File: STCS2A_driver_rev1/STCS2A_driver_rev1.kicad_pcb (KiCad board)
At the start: 2 copper layers, 80 x 60 mm, 38 parts, among them J1 Conn_01x04, J10 Screw_Terminal_01x02, J11 Screw_Terminal_01x02, J12 Screw_Terminal_01x02, J2 Conn_01x02, J3 Conn_01x04, J4 Screw_Terminal_01x02, J5 Screw_Terminal_01x02, J6 Conn_01x04, J7 Screw_Terminal_01x02, J8 Screw_Terminal_01x02, J9 Screw_Terminal_01x02, Q1 IRF9540N, U1 STCS2A, U2 STCS2A, U3 STCS2A, U4 STCS2A

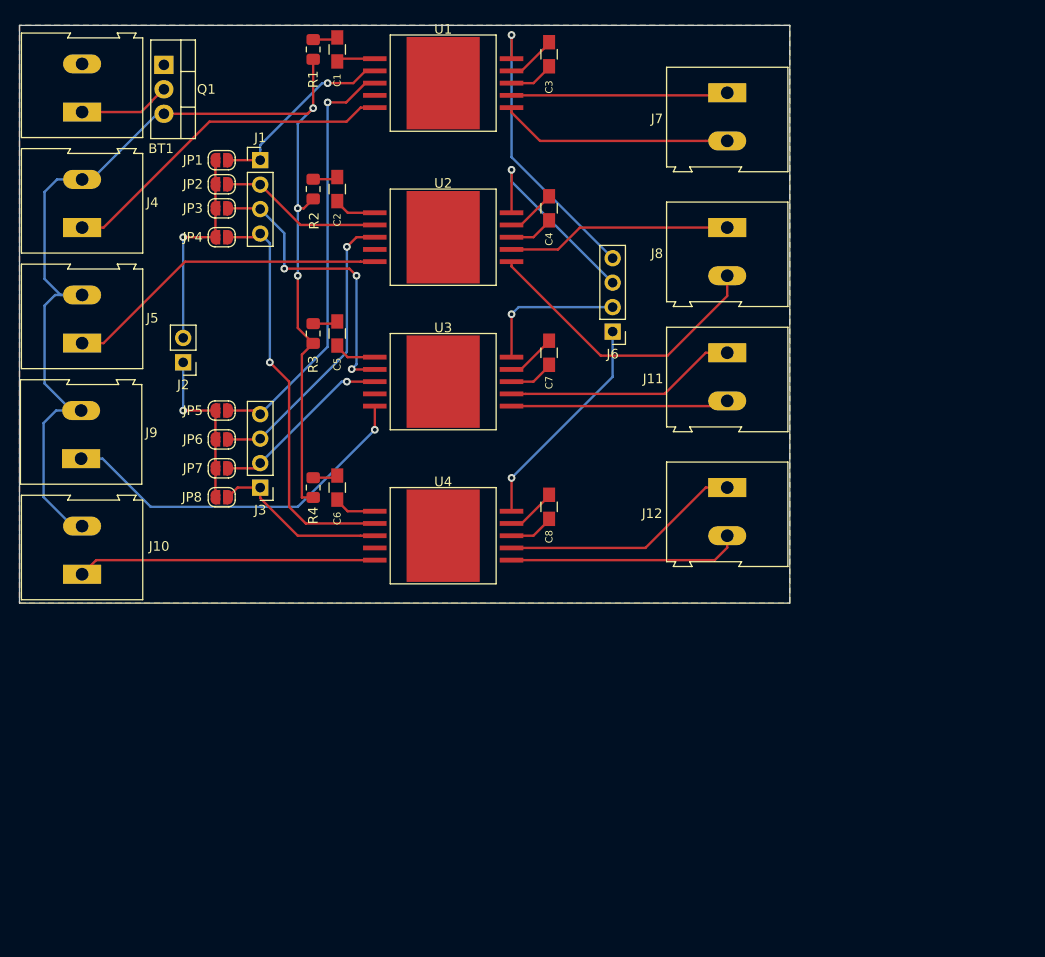
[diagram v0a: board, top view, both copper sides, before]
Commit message: Finished STCS2A driver board
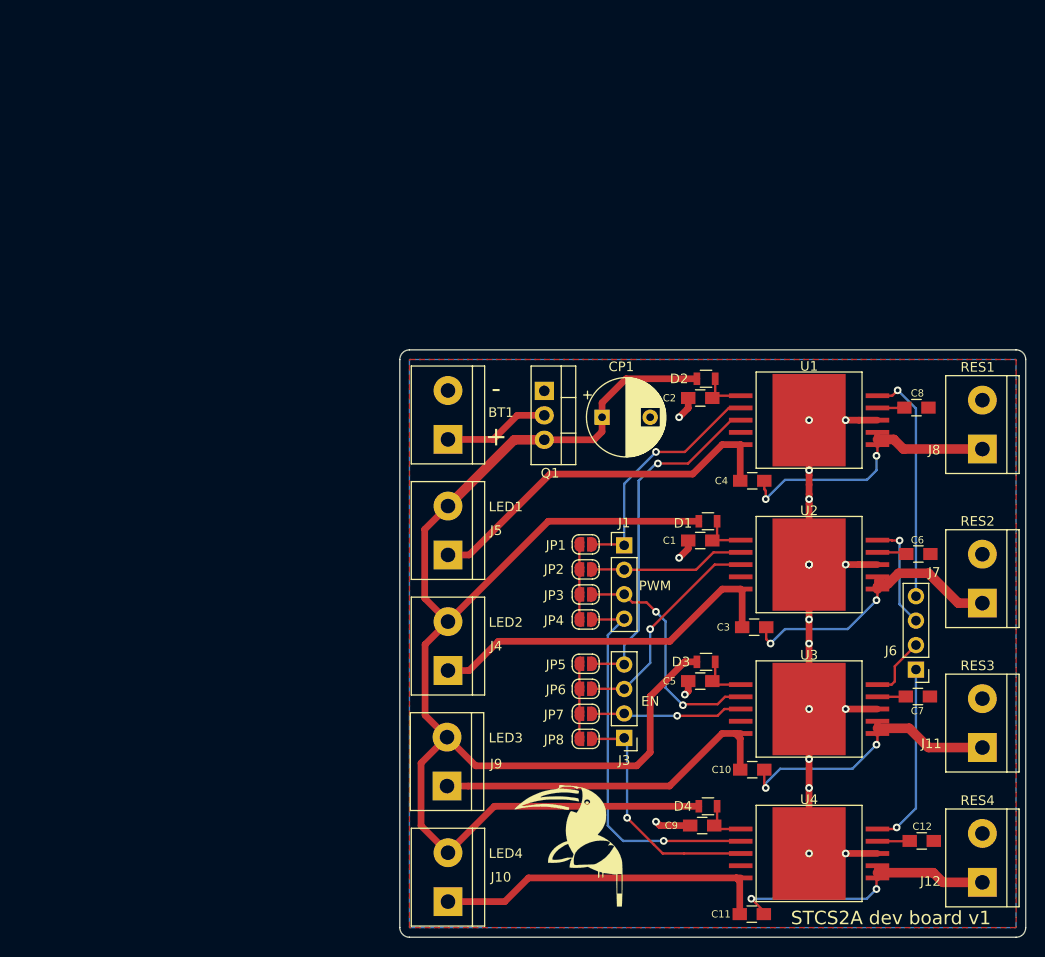
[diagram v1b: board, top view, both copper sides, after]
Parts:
- removed J2: Conn_01x02, Connector_PinHeader_2.54mm:PinHeader_1x02_P2.54mm_Vertical
- removed R1, R2, R3, R4: R, Resistor_SMD:R_0805_2012Metric_Pad1.15x1.40mm_HandSolder
- added C10: 0.47uF, sense_fp:C_0805_HandSoldering, F.Cu at (86.1, 87.3)
- added C11: 0.47uF, sense_fp:C_0805_HandSoldering, F.Cu at (86.0, 102.3)
- added C12: 8pF, sense_fp:C_0805_HandSoldering, F.Cu at (103.7, 94.7)
- added C9: 0.1uF, sense_fp:C_0805_HandSoldering, F.Cu at (80.9, 93.1)
- added CP1: 100uF, sense_fp:CP_Radial_D8.0mm_P5.00mm, F.Cu at (70.5, 50.7)
- added D1: BAT46, sense_fp:R_0805, F.Cu at (81.5, 61.5)
- added D2: BAT46, sense_fp:R_0805, F.Cu at (81.3, 46.7)
- added D3: BAT46, sense_fp:R_0805, F.Cu at (81.3, 76.1)
- added D4: BAT46, sense_fp:R_0805, F.Cu at (81.5, 91.1)
- added G***: Appiko_LOGO_img, sense_fp:Appiko_LOGO_img, F.Cu at (67.0, 95.2)
- BT1: value Battery_Cell -> Battery; footprint TerminalBlock:TerminalBlock_Altech_AK300-2_P5.00mm -> sense_fp:TerminalBlock_bornier-2_P5.08mm
- C1, C2, C5: footprint sense:C_0805_HandSoldering -> sense_fp:C_0805_HandSoldering
- C3, C4: value 10nF -> 0.47uF; footprint sense:C_0805_HandSoldering -> sense_fp:C_0805_HandSoldering
- C6: value 0.1uF -> 8pF; footprint sense:C_0805_HandSoldering -> sense_fp:C_0805_HandSoldering
- C7, C8: value 10nF -> 8pF; footprint sense:C_0805_HandSoldering -> sense_fp:C_0805_HandSoldering
- J1, J3, J6: footprint Connector_PinHeader_2.54mm:PinHeader_1x04_P2.54mm_Vertical -> sense_fp:PinHeader_1x04_P2.54mm_Vertical
- J10, J11, J12, J4, J5, J7, J8, J9: footprint TerminalBlock:TerminalBlock_Altech_AK300-2_P5.00mm -> sense_fp:TerminalBlock_bornier-2_P5.08mm
- JP1, JP2, JP3, JP4, JP5, JP6, JP7, JP8: footprint Jumper:SolderJumper-2_P1.3mm_Open_RoundedPad1.0x1.5mm -> sense_fp:SolderJumper-2_P1.3mm_Open_RoundedPad1.0x1.5mm
- Q1: value IRF9540N -> IRF9540; footprint Package_TO_SOT_THT:TO-220-3_Vertical -> sense_fp:TO-220-3_Vertical
- U1, U2, U3, U4: footprint sense:STCS2A_PowerSO-10 -> sense_fp:STCS2A_PowerSO-10
- moved C1 63.4 mm to (80.7, 63.5), turned to 0 degrees
- moved C3 63.2 mm to (86.3, 72.5), turned to 0 degrees
- moved C6 60.7 mm to (103.3, 64.9), turned to 0 degrees
- moved J4 59.7 mm to (54.5, 77.0)
- moved J7 59.3 mm to (110.0, 70.0), turned to 90 degrees
- moved JP3 55.1 mm to (68.8, 69.1)
- moved J1 55.0 mm to (72.8, 64.0)
- moved JP2 55.0 mm to (68.8, 66.5)
- moved JP1 55.0 mm to (68.8, 63.9)
- moved JP4 54.8 mm to (68.8, 71.7)
- moved C7 52.4 mm to (103.3, 79.7), turned to 0 degrees
- moved C5 52.2 mm to (80.7, 78.1), turned to 0 degrees
- moved Q1 52.0 mm to (64.5, 48.0)
- moved U1 51.7 mm to (92.0, 51.0)
- moved BT1 51.0 mm to (54.5, 53.0)
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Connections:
- net /EN renamed Net-(JP5-Pad2)
- net /PWM renamed Net-(JP1-Pad1)
- net Net-(J10-Pad1) renamed /LED4
- net Net-(J9-Pad1) renamed /LED3
- net VCC renamed VDD
- C1 pad 1: Net-(C1-Pad1) -> GND
- C2 pad 1: Net-(C2-Pad1) -> GND
- C3 pad 1: Net-(C3-Pad1) -> /LED2
- C3 pad 2: GND -> /RES2
- C4 pad 1: Net-(C4-Pad1) -> /LED1
- C4 pad 2: GND -> /RES1
- C5 pad 1: Net-(C5-Pad1) -> GND
- C6 pad 2: Net-(C6-Pad2) -> GND
- J11 pad 1: Net-(J11-Pad1) -> /RES3
- J11 pad 2: Net-(J11-Pad2) -> GND
- J12 pad 1: Net-(J12-Pad1) -> /RES4
- J12 pad 2: Net-(J12-Pad2) -> GND
- J4 pad 1: Net-(J4-Pad1) -> /LED2
- J5 pad 1: Net-(J5-Pad1) -> /LED1
- J7 pad 1: Net-(J7-Pad1) -> /RES2
- J7 pad 2: Net-(J7-Pad2) -> GND
- J8 pad 1: Net-(J8-Pad1) -> /RES1
- J8 pad 2: Net-(J8-Pad2) -> GND
- U1 pad 1: Net-(C1-Pad1) -> Net-(C2-Pad2)
- U1 pad 5: Net-(J4-Pad1) -> /LED1
- U1 pad 6: Net-(J7-Pad2) -> /RES1
- U1 pad 7: Net-(J7-Pad1) -> /RES1
- U1 pad 9: Net-(C3-Pad1) -> Net-(C8-Pad1)
- U2 pad 1: Net-(C2-Pad1) -> Net-(C1-Pad2)
- U2 pad 5: Net-(J5-Pad1) -> /LED2
- U2 pad 6: Net-(J8-Pad2) -> /RES2
- U2 pad 7: Net-(J8-Pad1) -> /RES2
- U2 pad 9: Net-(C4-Pad1) -> Net-(C6-Pad1)
- U3 pad 1: Net-(C5-Pad1) -> Net-(C5-Pad2)
- U3 pad 6: Net-(J11-Pad2) -> /RES3
- U3 pad 7: Net-(J11-Pad1) -> /RES3
- U4 pad 1: Net-(C6-Pad1) -> Net-(C9-Pad2)
- U4 pad 6: Net-(J12-Pad2) -> /RES4
- U4 pad 7: Net-(J12-Pad1) -> /RES4
- U4 pad 9: Net-(C8-Pad1) -> Net-(C12-Pad1)
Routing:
- net GND: track 18.8 -> 83.2 mm, vias 0 -> 19
- net /LED1: track 0.00 -> 38.9 mm
- net VDD: track 130.4 -> 168.8 mm, vias 3 -> 0
- net /LED2: track 0.00 -> 37.9 mm
- net Net-(J4-Pad1): track 35.6 -> 0.00 mm
- net Net-(J5-Pad1): track 33.9 -> 0.00 mm
- net Net-(J8-Pad2): track 31.4 -> 0.00 mm
- net /RES2: track 0.00 -> 29.9 mm, vias 0 -> 2
- net /RES1: track 0.00 -> 29.7 mm, vias 0 -> 2
- net /RES3: track 0.00 -> 29.6 mm, vias 0 -> 2
- net /RES4: track 0.00 -> 29.0 mm, vias 0 -> 2
- net Net-(J12-Pad1): track 25.0 -> 0.00 mm
- net Net-(J12-Pad2): track 24.2 -> 0.00 mm
- net Net-(J11-Pad1): track 24.2 -> 0.00 mm
- net Net-(J7-Pad2): track 24.1 -> 0.00 mm
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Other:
- board size 80 x 60 mm -> 65 x 61 mm
- net class Power added: clearance 0.2, trace_width 0.7, via_dia 0.8, via_drill 0.4
- board text added: "+"
- board text added: "-"
- board text added: "EN"
- board text added: "LED1"
- board text added: "LED2"
- board text added: "LED3"
- board text added: "LED4"
- board text added: "PWM"
- board text added: "RES1"
- board text added: "RES2"
- board text added: "RES3"
- board text added: "RES4"
- board text added: "STCS2A dev board v1"
